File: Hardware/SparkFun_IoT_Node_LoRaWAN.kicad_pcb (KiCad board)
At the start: 4 copper layers, 59 x 82 mm, 213 parts, among them J1 Conn_01x03, J2 JST_2mm_LiPo, J3 Qwiic_RA, J4 USB_C_Receptacle, J5 USB_C_Receptacle, J6 SWD, J7 Conn_01x12, J8 Conn_01x12, J9 microSD_Friction, Q1 RE1C002UNTCL, Q2 RE1C002UNTCL, SW1 SMD_4.6x2.8mm_h2.5mm, SW2 SMD_4.6x2.8mm_h2.5mm, SW3 DPDT_Slide_SMD_7.2x3.5mm, SW4 PTH_RA_h7.5mm, U3 CH340C, U4 W25Q128JVPIM, U5 LM66200, U6 RT9080-3.3, U7 MCP73831, U8 MAX17048, U9 RT9080-3.3

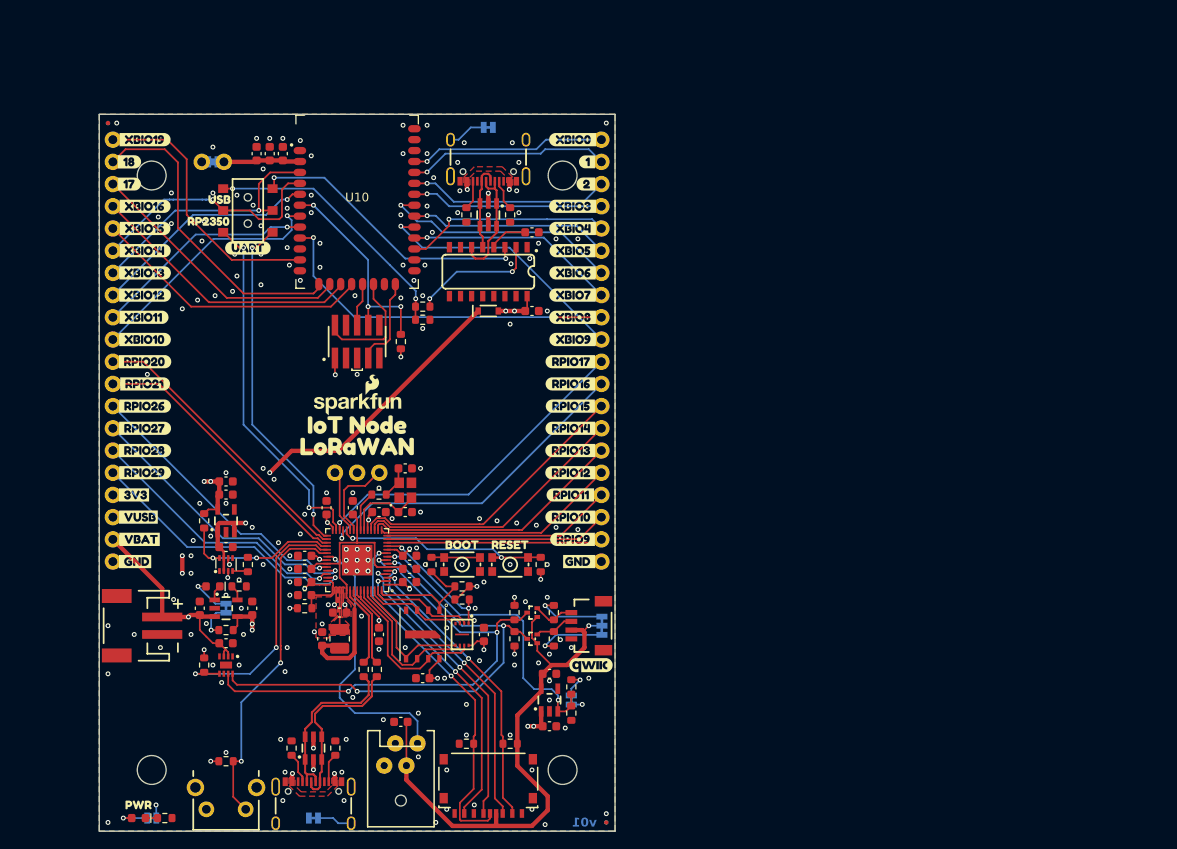
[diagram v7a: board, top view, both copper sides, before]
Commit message: v02 Board Updates
Still in progress...

Bump version number to v02
Update RP2350, APS6404L, and 12MHz crystal footprints
Move USB-C connector to be centered, and not go through wall of enclosure
Move power LED and RGB LED to be symmetric along south edge of board
Move battery connector, Qwiic connector, and uSD card connector to middle edges of board
Move IoT Node headers south
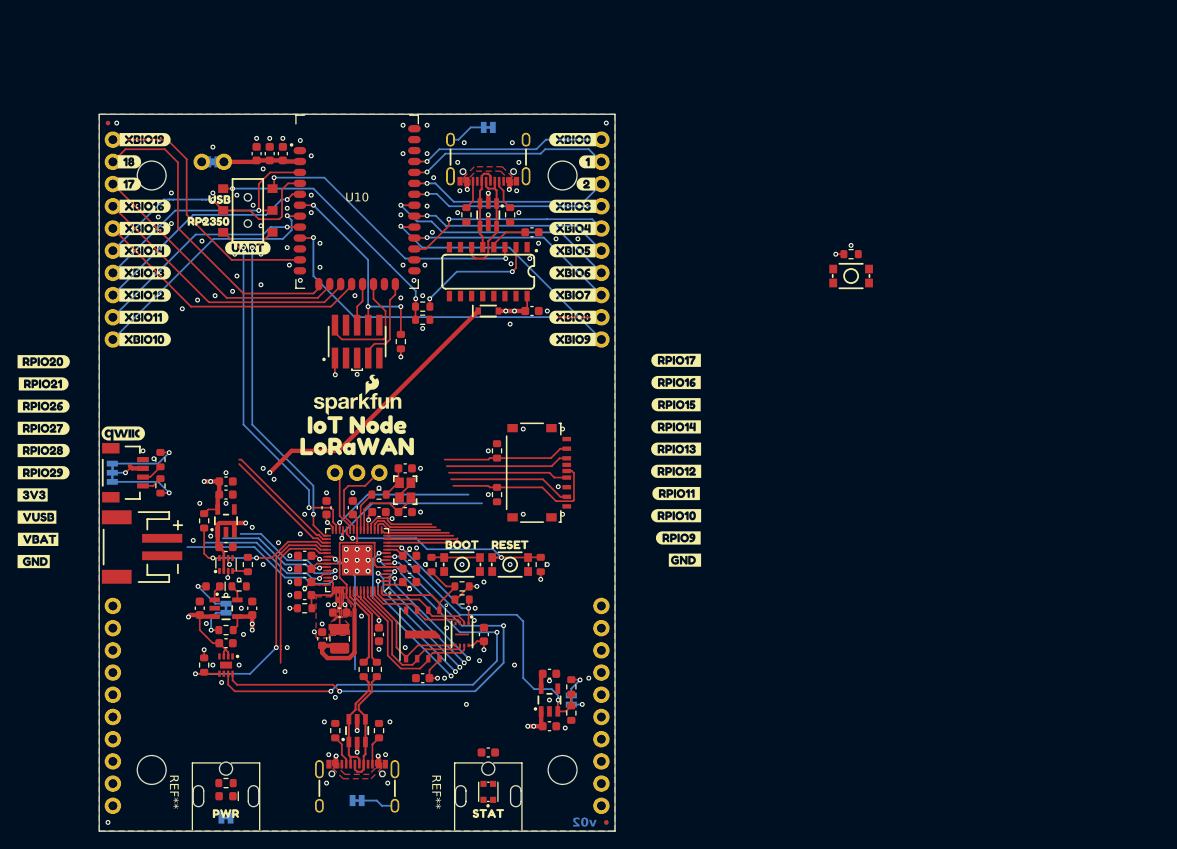
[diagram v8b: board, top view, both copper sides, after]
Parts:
- removed Q1, Q2: RE1C002UNTCL, SparkFun-Semiconductor-Standard:SC-89 SOT-490
- removed R27, R28: 2.2k, SparkFun-Resistor:R_0603_1608Metric
- added J10: Conn_01x10, SparkFun-Connector:1x10, F.Cu at (72.1, 138.1)
- added J11: Conn_01x10, SparkFun-Connector:1x10, F.Cu at (127.9, 138.1)
- added REF**: SMD-CBI, SparkFun-LED:SMD-CBI, F.Cu at (115.0, 136.5)
- added REF**: SMD-CBI, SparkFun-LED:SMD-CBI, F.Cu at (85.0, 136.5)
- added kibuzzard-66999523: G***, kibuzzard-66999523, F.Cu at (115.0, 139.0)
- D1: footprint SparkFun-LED:WS2812B-CBI -> SparkFun-LED:WS2812-2020
- J7, J8: value Conn_01x12 -> Conn_01x10; footprint SparkFun-Connector:1x20 -> SparkFun-Connector:1x10
- SW4: value PTH_RA_h7.5mm -> SMD_4.6x2.8mm_h2.5mm; footprint SparkFun-Switch:Push_PTH_RA_8-020_h7.5mm -> SparkFun-Switch:Push_SMD_4.6x2.8mm
- U1: value ~ -> RP2350A; footprint RP2350A:RP2350A -> SparkFun_IoT_Node_LoRaWAN:RP2350A
- U10: value ~ -> XBLR
- U2: value ~ -> APS6404L-3SQR-ZR; footprint RP2350A:APS6404L-3SQR-ZR -> SparkFun-Semiconductor-Standard:USON-8_3x2mm-SkinnyCenterPad
- Y1: value ~ -> 12MHz; footprint SparkFun-Clocks:CRYSTAL-SMD-2X2.5MM -> SparkFun-Clock:Crystal_SMD_2.5x2.0mm
- moved SW4 94.0 mm to (156.5, 77.5)
- moved R21 92.1 mm to (156.5, 75.0)
- moved G*** 59.7 mm to (73.2, 95.5)
- moved JP4 58.7 mm to (72.0, 100.0), turned to 90 degrees
- moved kibuzzard-6691B73B 55.3 mm to (73.8, 100.0), turned to -90 degrees
- moved J3 52.0 mm to (75.5, 100.0), turned to -90 degrees
- moved R13 49.4 mm to (77.5, 98.5), turned to -90 degrees
- moved R20 47.3 mm to (77.5, 101.5), turned to 90 degrees
- moved J9 35.4 mm to (120.0, 100.0), turned to 90 degrees
- moved R26 33.5 mm to (116.0, 97.5), turned to -90 degrees
- moved R5 28.7 mm to (116.0, 102.5), turned to -90 degrees
- moved kibuzzard-6691B338 12.1 mm to (136.5, 87.1)
- moved kibuzzard-6691B363 12.1 mm to (136.5, 99.8)
- moved kibuzzard-6691B36B 12.1 mm to (136.5, 89.7)
- moved kibuzzard-6691B36F 12.1 mm to (136.5, 92.2)
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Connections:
- net /RP2350/USB_D+ renamed /USB_D+
- net /RP2350/USB_D- renamed /USB_D-
- net Net-(JP6-B) renamed 3.3V_XBLR
- C29 pad 2: Net-(Y1-1) -> Net-(C29-Pad2)
- D1 pad 1: LED_IN -> LED_OUT
- D1 pad 2: 3.3V_P -> GND
- D1 pad 3: GND -> LED_IN
- D1 pad 4: LED_OUT -> 3.3V_P
- J3 pad 2: 3.3V_P -> 3.3V
- J3 pad 3: SDA_OUT -> SDA
- J3 pad 4: SCL_OUT -> SCL
- J6 pad 10: (no net) -> XBLR_~{RESET}
- J6 pad 2: XBLR_SWO -> XBLR_SWDIO
- J6 pad 3: (no net) -> GND
- J6 pad 4: (no net) -> XBLR_SWCLK
- J6 pad 6: XBLR_SWCLK -> XBLR_SWO
- J6 pad 7: XBLR_SWDIO -> (no net)
- J6 pad 8: XBLR_~{RESET} -> (no net)
- J6 pad 9: (no net) -> GND
- JP4 pad 2: 3.3V_P -> 3.3V
- R13 pad 2: SDA_OUT -> SDA
- R20 pad 2: SCL_OUT -> SCL
- R25 pad 2: Net-(Y1-1) -> Net-(C29-Pad2)
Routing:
- net 3.3V_P: track 63.9 -> 1.77 mm, vias 1 -> 0
- net RP2350_IO15: track 33.2 -> 8.33 mm
- net RP2350_IO14: track 31.7 -> 8.11 mm
- net RP2350_IO13: track 30.2 -> 8.01 mm
- net RP2350_IO17: track 38.4 -> 16.9 mm
- net RP2350_IO26: track 32.2 -> 11.5 mm
- net RP2350_IO12: track 28.1 -> 7.83 mm
- net USER_BUTTON: track 38.1 -> 18.0 mm, vias 2 -> 0
- net RP2350_IO16: track 38.3 -> 19.0 mm
- net RP2350_IO20: track 32.9 -> 13.8 mm
- net RP2350_IO11: track 26.4 -> 7.56 mm
- net RP2350_IO21: track 32.0 -> 13.8 mm
- net RP2350_IO27: track 33.4 -> 15.6 mm
- net RP2350_IO10: track 25.5 -> 8.10 mm
- net LED_IN: track 31.6 -> 15.1 mm
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- added copper zone on F.Cu, net (none)
- removed copper zone on F.Cu, net Net-(U1-VREG_LX)
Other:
- board text added: "v02"
- board text removed: "v01"
